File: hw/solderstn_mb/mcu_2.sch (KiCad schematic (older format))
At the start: 4 parts

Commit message: Summer vacation 2020 updates: * Front panel design rev 1 complete (incl Experimental outer board with optional linear touch sensors) * MB schematics AlmostDone(tm) - 'old' pinout supporting only one Rotary encoder * Lots of docs for new stuff
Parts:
- removed C?: C_Small, symbol Device:C_Small
- removed FB?: Ferrite_Bead_Small, symbol customlib_mj:Ferrite_Bead_Small
- removed R?: R_Small, symbol Device:R_Small
- added C401: 10u, symbol Device:C_Small
- added C402, C403, C404, C405, C406, C407, C408, C411, C416, C417: 100n, symbol Device:C_Small
- added C409, C410: 2u2, symbol Device:C_Small
- added C412, C413, C415: 1u, symbol Device:C_Small
- added C414: 22u, symbol Device:C_Small
- added NT401: Net-Tie_2, symbol Device:Net-Tie_2
- added U402: REF6125IDGK, Package_SO:VSSOP-8_3.0x3.0mm_P0.65mm, symbol customlib_mj:REF6125IDGK
- added U403: TLV9052SIDGS, Package_SO:VSSOP-10_3x3mm_P0.5mm, symbol customlib_mj:TLV9052SIDGS
- gave numbers to parts that had none: 1
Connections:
- net GND: now also U401.10 (VSS), U401.27 (VSS), U401.74 (VSS), U401.99 (VSS), C401.2, C402.2, C403.2, C404.2, C405.2, C406.2, C407.2, C408.2, C409.2, C410.2, NT401.1
- net VDD: now also U401.100 (VDD), U401.11 (VDD), U401.19 (VDD), U401.28 (VDD), U401.50 (VDD), U401.6 (VBAT), U401.75 (VDD), C401.1, C402.1, C403.1, C404.1, C405.1, C406.1, C407.1, C408.1
- net GNDA: now reaches U401.20 (VSSA)
- net GNDA: now also C411.2, C412.2, C413.1, C414.2, C415.2, C416.2, C417.2, NT401.2, U402.7 (GND_F), U402.8 (GND_S)
- net Vref_2v5: now reaches U401.21 (VREF+)
- net Vref_2v5: now also C414.1, C415.1, C416.1, U402.5 (OUT_S), U402.6 (OUT_F), U403.3 (+), U403.7 (+)
- net VDDA: now reaches U401.22 (VDDA)
- net VDDA: now also C411.1, C412.1, C417.1, U402.1 (VIN), U402.2 (EN), U402.3 (SS)
- net at U401.49 (VCAP_1): now also C410.1
- net at U401.73 (VCAP_2): now also C409.1
- new net: C413.2, U402.4 (FILT)
- new net KTY_BIAS_CH_A: U403.1, U403.2 (-)
- new net KTY_BIAS_CH_B: U403.8 (-), U403.9
- new net KTY_BIAS_EN: U403.5 (~SHDN~), U403.6 (~SHDN~)
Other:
- note added: "MCU decoupling - place close to MCU power pins"
- note added: "Precisin Vref. Place close\nto MCU. See REF6125 ds\nfor layout suggestions."
- note added: "Switchable Vref for biasing KTY sensors\n(for cold-junction compensation), one\nper channel. The KTY's can then be\nmeassured through the ordinary TC \namps.\n"
- moved on the sheet: U401C

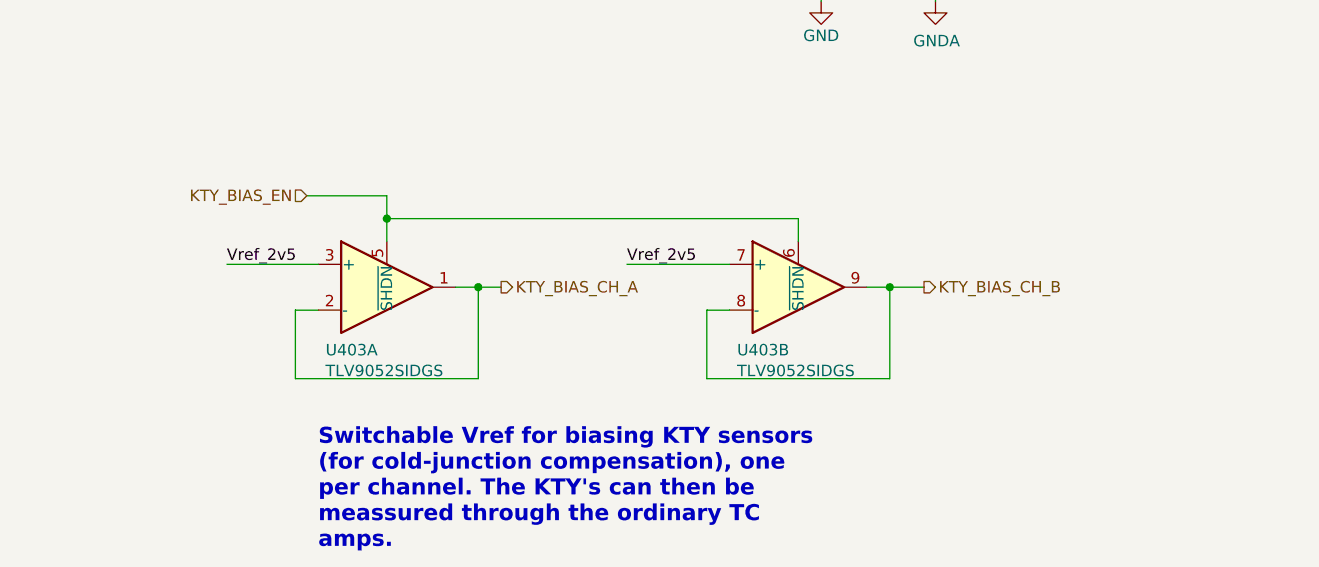
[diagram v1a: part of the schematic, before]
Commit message: Update pinout to "alternative", shuffling stuff around to optionally support a 2nd rotary on front-panel (corresponding Front-panel side not yet updated)
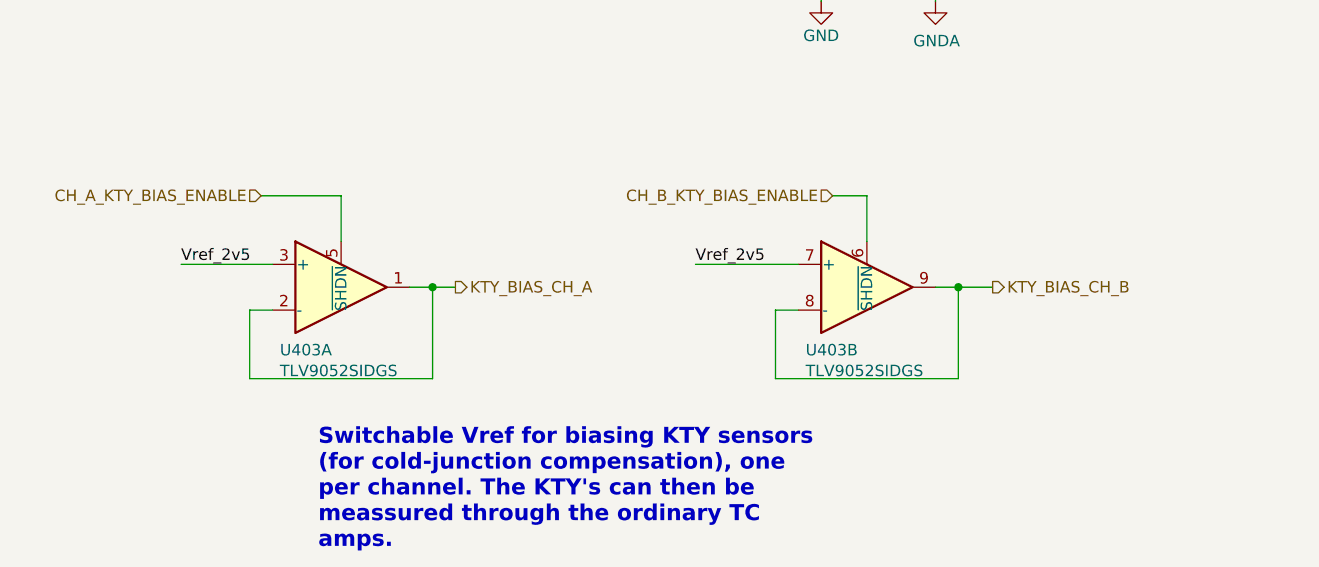
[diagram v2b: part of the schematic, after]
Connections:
- net KTY_BIAS_EN renamed CH_A_KTY_BIAS_ENABLE
- net CH_A_KTY_BIAS_ENABLE: no longer U403.6 (~SHDN~)
- new net CH_B_KTY_BIAS_ENABLE: U403.6 (~SHDN~)
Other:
- moved on the sheet: U403A, U403B
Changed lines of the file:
@@
 L customlib_mj:TLV9052SIDGS U?
 U 1 1 5F392B98
-P 3350 5900
+P 3150 5900
 AR Path="/5F785D6E/5F392B98" Ref="U?"  Part="1"
 AR Path="/5EAEB4B5/5F392B98" Ref="U403"  Part="1"
-F 0 "U403" H 3082 5625 50  0000 L CNN
-F 1 "TLV9052SIDGS" H 3082 5534 50  0000 L CNN
-F 2 "Package_SO:VSSOP-10_3x3mm_P0.5mm" H 3350 5900 50  0001 C CNN
-F 3 "https://www.ti.com/lit/gpn/tlv9052" H 3400 6100 50  0001 C CNN
-	1    3350 5900
+F 0 "U403" H 2882 5625 50  0000 L CNN
+F 1 "TLV9052SIDGS" H 2882 5534 50  0000 L CNN
+F 2 "Package_SO:VSSOP-10_3x3mm_P0.5mm" H 3150 5900 50  0001 C CNN
+F 3 "https://www.ti.com/lit/gpn/tlv9052" H 3200 6100 50  0001 C CNN
+	1    3150 5900
 	1    0    0    -1
 $EndComp
@@
 L customlib_mj:TLV9052SIDGS U?
 U 2 1 5F392B9E
-P 5150 5900
+P 5450 5900
 AR Path="/5F785D6E/5F392B9E" Ref="U?"  Part="2"
 AR Path="/5EAEB4B5/5F392B9E" Ref="U403"  Part="2"
-F 0 "U403" H 4882 5625 50  0000 L CNN
-F 1 "TLV9052SIDGS" H 4882 5534 50  0000 L CNN
-F 2 "Package_SO:VSSOP-10_3x3mm_P0.5mm" H 5150 5900 50  0001 C CNN
-F 3 "https://www.ti.com/lit/gpn/tlv9052" H 5200 6100 50  0001 C CNN
-	2    5150 5900
-	1    0    0    -1
-$EndComp
-Text HLabel 3000 5500 0    50   Input ~ 0
-KTY_BIAS_EN
-Wire Wire Line
-	3350 5500 3000 5500
-Wire Wire Line
-	3350 5600 5150 5600
-Wire Wire Line
-	5150 5600 5150 5700
-Wire Wire Line
-	3650 5900 3750 5900
-Wire Wire Line
-	3750 5900 3750 6300
-Wire Wire Line
-	3750 6300 2950 6300
-Wire Wire Line
-	2950 6300 2950 6000
-Wire Wire Line
-	2950 6000 3050 6000
-Wire Wire Line
-	5450 5900 5550 5900
-Wire Wire Line
-	5550 5900 5550 6300
-Wire Wire Line
-	5550 6300 4750 6300
-Wire Wire Line
-	4750 6300 4750 6000
-Wire Wire Line
-	4750 6000 4850 6000
-Wire Wire Line
-	3050 5800 2650 5800
-Wire Wire Line
-	4850 5800 4400 5800
-Text Label 4400 5800 0    50   ~ 0
+F 0 "U403" H 5182 5625 50  0000 L CNN
+F 1 "TLV9052SIDGS" H 5182 5534 50  0000 L CNN
+F 2 "Package_SO:VSSOP-10_3x3mm_P0.5mm" H 5450 5900 50  0001 C CNN
+F 3 "https://www.ti.com/lit/gpn/tlv9052" H 5500 6100 50  0001 C CNN
+	2    5450 5900
+	1    0    0    -1
+$EndComp
+Text HLabel 2800 5500 0    50   Input ~ 0
+CH_A_KTY_BIAS_ENABLE
+Wire Wire Line
+	3150 5500 2800 5500
+Wire Wire Line
+	3450 5900 3550 5900
+Wire Wire Line
+	3550 5900 3550 6300
+Wire Wire Line
+	3550 6300 2750 6300
+Wire Wire Line
+	2750 6300 2750 6000
+Wire Wire Line
+	2750 6000 2850 6000
+Wire Wire Line
+	5750 5900 5850 5900
+Wire Wire Line
+	5850 5900 5850 6300
+Wire Wire Line
+	5850 6300 5050 6300
+Wire Wire Line
+	5050 6300 5050 6000
+Wire Wire Line
+	5050 6000 5150 6000
+Wire Wire Line
+	2850 5800 2450 5800
+Wire Wire Line
+	5150 5800 4700 5800
+Text Label 4700 5800 0    50   ~ 0
 Vref_2v5
-Text Label 2650 5800 0    50   ~ 0
+Text Label 2450 5800 0    50   ~ 0
 Vref_2v5
 Wire Wire Line
-	5550 5900 5700 5900
-Connection ~ 5550 5900
-Wire Wire Line
-	3750 5900 3850 5900
-Connection ~ 3750 5900
-Wire Wire Line
-	3350 5500 3350 5600
-Connection ~ 3350 5600
-Wire Wire Line
-	3350 5600 3350 5700
+	5850 5900 6000 5900
+Connection ~ 5850 5900
+Wire Wire Line
+	3550 5900 3650 5900
+Connection ~ 3550 5900
 $Comp
 L Device:C_Small C414
@@
 Text Label 3900 3300 2    50   ~ 0
 Vref_2v5
-Text HLabel 3850 5900 2    50   Output ~ 0
+Text HLabel 3650 5900 2    50   Output ~ 0
 KTY_BIAS_CH_A
-Text HLabel 5700 5900 2    50   Output ~ 0
+Text HLabel 6000 5900 2    50   Output ~ 0
 KTY_BIAS_CH_B
 Wire Wire Line
@@
 Text Notes 3050 7050 0    70   ~ 14
 Switchable Vref for biasing KTY sensors\n(for cold-junction compensation), one\nper channel. The KTY's can then be\nmeassured through the ordinary TC \namps.\n
+Text HLabel 5300 5500 0    50   Input ~ 0
+CH_B_KTY_BIAS_ENABLE
+Wire Wire Line
+	3150 5500 3150 5700
+Wire Wire Line
+	5300 5500 5450 5500
+Wire Wire Line
+	5450 5500 5450 5700
 $EndSCHEMATC

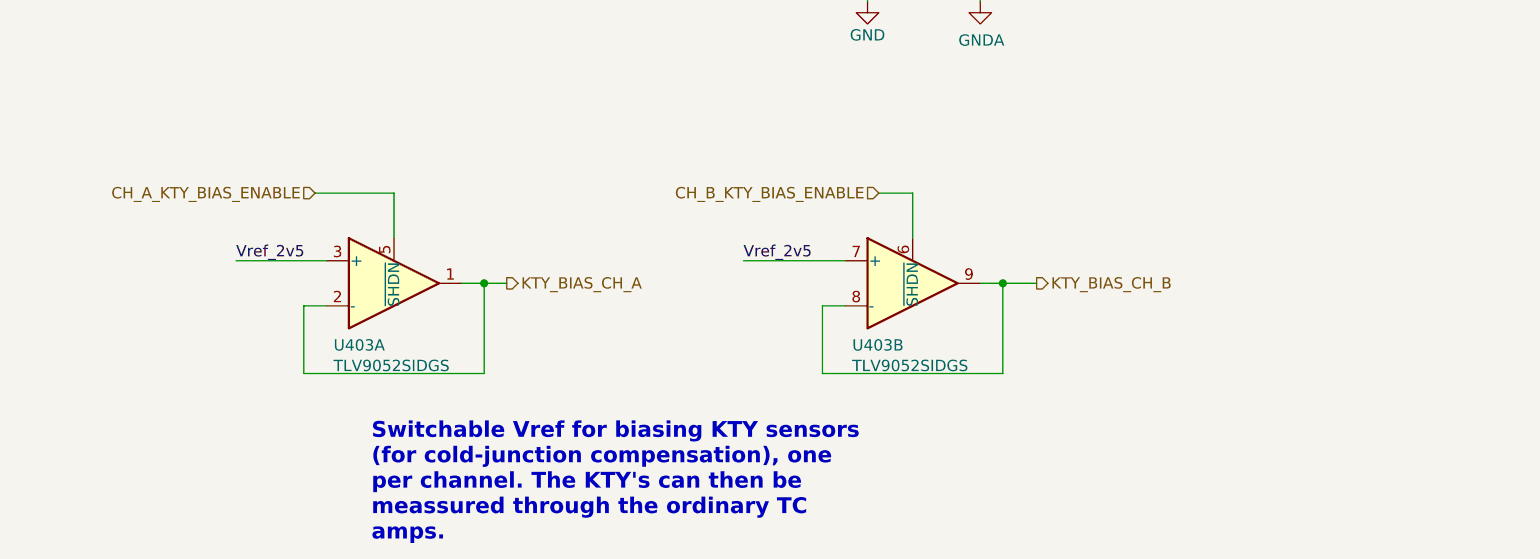
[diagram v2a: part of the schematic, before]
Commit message: * Remove separate REED_PULLUP_EN pin; instead bias the Reedswitches with the per-channel KTY bias (buffered Vref) * Add separate mini cut-out sub-PCB for 3.5 headphone connector at back-panel (must be angled vertical to fit in panel) * Some ESD and buffering on back panel
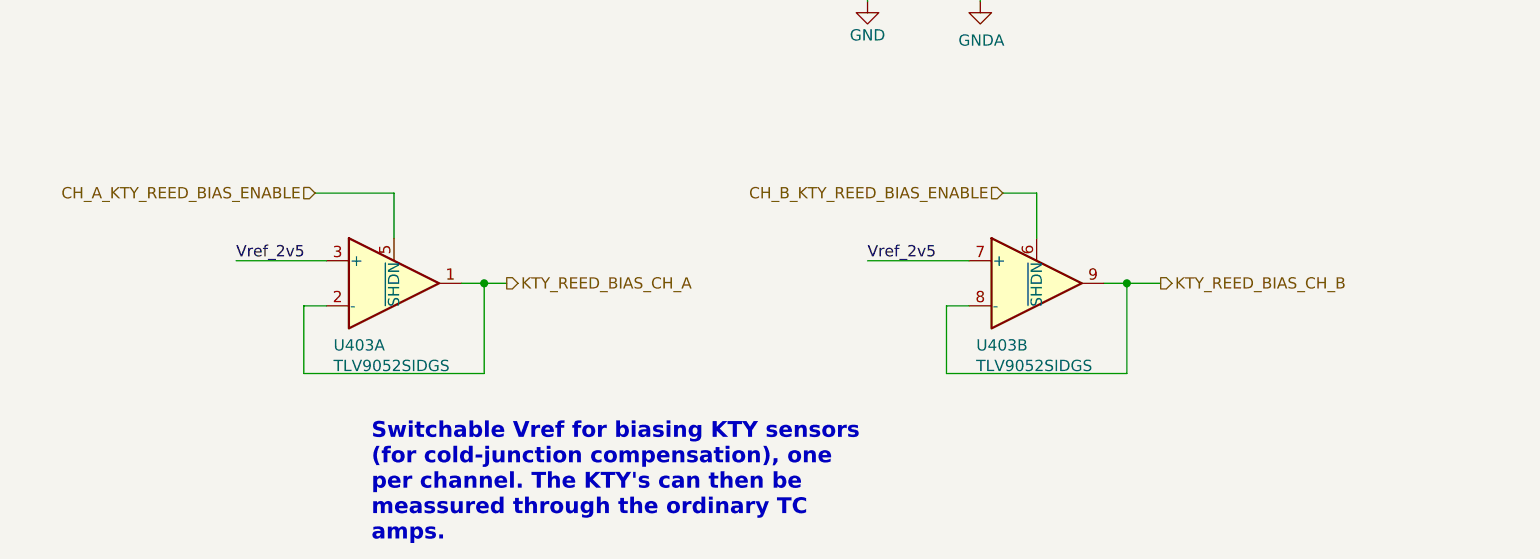
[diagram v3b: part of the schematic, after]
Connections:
- net CH_A_KTY_BIAS_ENABLE renamed CH_A_KTY_REED_BIAS_ENABLE
- net CH_B_KTY_BIAS_ENABLE renamed CH_B_KTY_REED_BIAS_ENABLE
- net KTY_BIAS_CH_A renamed KTY_REED_BIAS_CH_A
- net KTY_BIAS_CH_B renamed KTY_REED_BIAS_CH_B
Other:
- moved on the sheet: U403B
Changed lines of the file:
@@
 $Descr A4 11693 8268
 encoding utf-8
-Sheet 4 21
+Sheet 4 22
 Title "STM32F429 MCU power, decoupling, Vref"
 Date "2020-04-26"
@@
 L customlib_mj:TLV9052SIDGS U?
 U 2 1 5F392B9E
-P 5450 5900
+P 6000 5900
 AR Path="/5F785D6E/5F392B9E" Ref="U?"  Part="2"
 AR Path="/5EAEB4B5/5F392B9E" Ref="U403"  Part="2"
-F 0 "U403" H 5182 5625 50  0000 L CNN
-F 1 "TLV9052SIDGS" H 5182 5534 50  0000 L CNN
-F 2 "Package_SO:VSSOP-10_3x3mm_P0.5mm" H 5450 5900 50  0001 C CNN
-F 3 "https://www.ti.com/lit/gpn/tlv9052" H 5500 6100 50  0001 C CNN
-	2    5450 5900
+F 0 "U403" H 5732 5625 50  0000 L CNN
+F 1 "TLV9052SIDGS" H 5732 5534 50  0000 L CNN
+F 2 "Package_SO:VSSOP-10_3x3mm_P0.5mm" H 6000 5900 50  0001 C CNN
+F 3 "https://www.ti.com/lit/gpn/tlv9052" H 6050 6100 50  0001 C CNN
+	2    6000 5900
 	1    0    0    -1
 $EndComp
 Text HLabel 2800 5500 0    50   Input ~ 0
-CH_A_KTY_BIAS_ENABLE
+CH_A_KTY_REED_BIAS_ENABLE
 Wire Wire Line
 	3150 5500 2800 5500
@@
 	2750 6000 2850 6000
 Wire Wire Line
-	5750 5900 5850 5900
-Wire Wire Line
-	5850 5900 5850 6300
-Wire Wire Line
-	5850 6300 5050 6300
-Wire Wire Line
-	5050 6300 5050 6000
-Wire Wire Line
-	5050 6000 5150 6000
+	6300 5900 6400 5900
+Wire Wire Line
+	6400 5900 6400 6300
+Wire Wire Line
+	6400 6300 5600 6300
+Wire Wire Line
+	5600 6300 5600 6000
+Wire Wire Line
+	5600 6000 5700 6000
 Wire Wire Line
 	2850 5800 2450 5800
 Wire Wire Line
-	5150 5800 4700 5800
-Text Label 4700 5800 0    50   ~ 0
+	5700 5800 5250 5800
+Text Label 5250 5800 0    50   ~ 0
 Vref_2v5
 Text Label 2450 5800 0    50   ~ 0
 Vref_2v5
 Wire Wire Line
-	5850 5900 6000 5900
-Connection ~ 5850 5900
+	6400 5900 6550 5900
+Connection ~ 6400 5900
 Wire Wire Line
 	3550 5900 3650 5900
@@
 Vref_2v5
 Text HLabel 3650 5900 2    50   Output ~ 0
-KTY_BIAS_CH_A
-Text HLabel 6000 5900 2    50   Output ~ 0
-KTY_BIAS_CH_B
+KTY_REED_BIAS_CH_A
+Text HLabel 6550 5900 2    50   Output ~ 0
+KTY_REED_BIAS_CH_B
 Wire Wire Line
 	6200 2700 6350 2700
@@
 Text Notes 3050 7050 0    70   ~ 14
 Switchable Vref for biasing KTY sensors\n(for cold-junction compensation), one\nper channel. The KTY's can then be\nmeassured through the ordinary TC \namps.\n
-Text HLabel 5300 5500 0    50   Input ~ 0
-CH_B_KTY_BIAS_ENABLE
+Text HLabel 5850 5500 0    50   Input ~ 0
+CH_B_KTY_REED_BIAS_ENABLE
 Wire Wire Line
 	3150 5500 3150 5700
 Wire Wire Line
-	5300 5500 5450 5500
-Wire Wire Line
-	5450 5500 5450 5700
+	5850 5500 6000 5500
+Wire Wire Line
+	6000 5500 6000 5700
 $EndSCHEMATC
